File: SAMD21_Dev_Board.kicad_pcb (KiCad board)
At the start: 2 copper layers, 55.4 x 87.4 mm, 88 parts, among them J1 SWD, J10 JST_SH_SM06B-SRSS-TB_1x06-1MP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, J11 JST_SH_SM06B-SRSS-TB_1x06-1MP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, J12 JST_SH_SM06B-SRSS-TB_1x06-1MP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, J13 JST_SH_SM06B-SRSS-TB_1x06-1MP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, J14 JST_SH_SM06B-SRSS-TB_1x06-1MP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, J15 JST_SH_SM06B-SRSS-TB_1x06-1MP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, J16 JST_SH_SM06B-SRSS-TB_1x06-1MP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, J17 Status LED, J2 USB_C_Receptacle_USB2.0_16P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

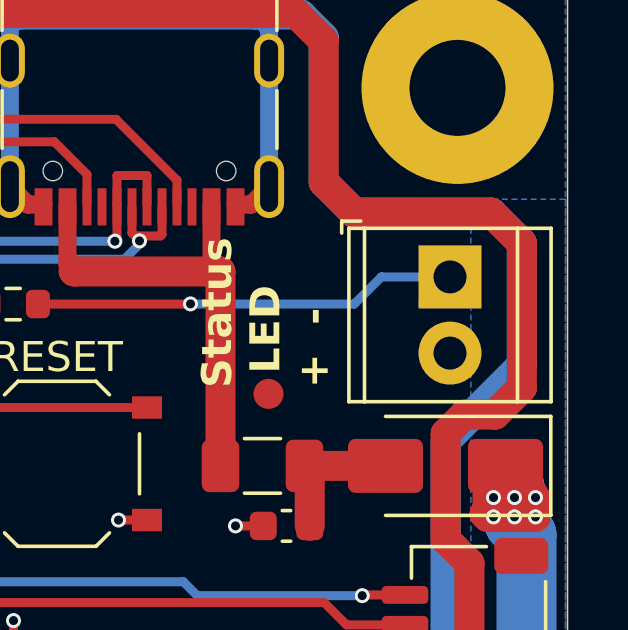
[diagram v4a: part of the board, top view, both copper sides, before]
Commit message: Increase solder paste opennings by 5% for elect.capacitor and headers. Decrease screw terminal holes from 1.1mm to 1.0mm.
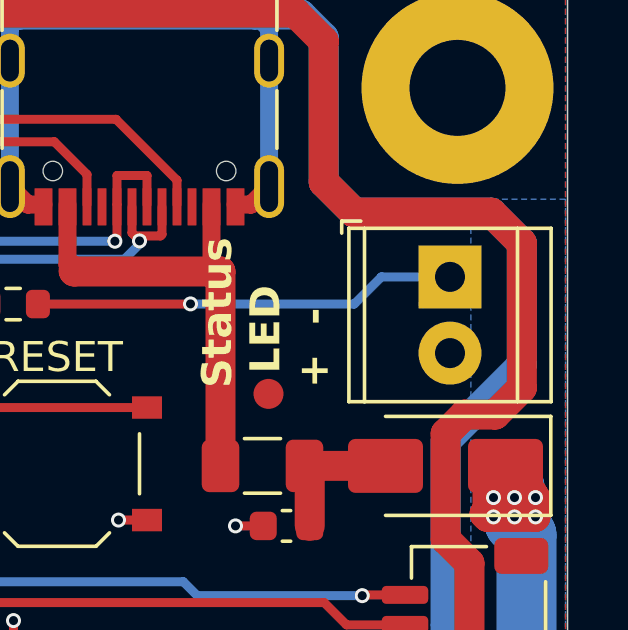
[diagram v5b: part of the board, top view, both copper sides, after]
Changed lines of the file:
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@@
 	(net 72 "D23")
 	(net 73 "D38")
-	(net 74 "unconnected-(J3-Pin_1-Pad1)_1")
-	(net 75 "unconnected-(J4-Pin_3-Pad3)")
-	(net 76 "unconnected-(J5-Pin_3-Pad3)")
-	(net 77 "unconnected-(J6-Pin_3-Pad3)")
-	(net 78 "unconnected-(J20-Pin_3-Pad3)")
-	(net 79 "unconnected-(J4-Pin_3-Pad3)_1")
-	(net 80 "unconnected-(J5-Pin_3-Pad3)_1")
-	(net 81 "unconnected-(J6-Pin_3-Pad3)_1")
-	(net 82 "unconnected-(J20-Pin_3-Pad3)_1")
-	(net 83 "unconnected-(J3-Pin_1-Pad1)")
-	(net 84 "unconnected-(J3-Pin_1-Pad1)_2")
-	(net 85 "D22")
-	(net 86 "D31")
+	(net 74 "unconnected-(J5-Pin_3-Pad3)")
+	(net 75 "unconnected-(J6-Pin_3-Pad3)")
+	(net 76 "unconnected-(J4-Pin_3-Pad3)_1")
+	(net 77 "unconnected-(J20-Pin_3-Pad3)_1")
+	(net 78 "unconnected-(J3-Pin_1-Pad1)")
+	(net 79 "D22")
+	(net 80 "D31")
 	(footprint "Capacitor_SMD:C_0603_1608Metric"
 		(layer "F.Cu")
@@
 			(layers "F.Cu" "F.Paste" "F.Mask")
 			(roundrect_rratio 0.25)
-			(net 85 "D22")
+			(net 79 "D22")
 			(pinfunction "Pin_6")
 			(pintype "passive")
@@
 			(at 0 0 270)
 			(size 2.1 2.1)
-			(drill 1.1)
+			(drill 1)
 			(layers "*.Cu" "*.Mask" "In1.Cu" "In2.Cu" "In3.Cu" "In4.Cu" "In5.Cu" "In6.Cu"
 				"In7.Cu" "In8.Cu" "In9.Cu" "In10.Cu" "In11.Cu" "In12.Cu" "In13.Cu" "In14.Cu"
@@
 			(at 2.54 0 270)
 			(size 2.1 2.1)
-			(drill 1.1)
+			(drill 1)
 			(layers "*.Cu" "*.Mask" "In1.Cu" "In2.Cu" "In3.Cu" "In4.Cu" "In5.Cu" "In6.Cu"
 				"In7.Cu" "In8.Cu" "In9.Cu" "In10.Cu" "In11.Cu" "In12.Cu" "In13.Cu" "In14.Cu"
@@
 			(layers "F.Cu" "F.Paste" "F.Mask")
 			(roundrect_rratio 0.25)
-			(net 85 "D22")
+			(net 79 "D22")
 			(pinfunction "PA12")
 			(pintype "bidirectional")
@@
 			(layers "F.Cu" "F.Paste" "F.Mask")
 			(roundrect_rratio 0.25)
-			(net 86 "D31")
+			(net 80 "D31")
 			(pinfunction "PB23")
 			(pintype "bidirectional+no_connect")
@@
 		(sheetname "Root")
 		(sheetfile "SAMD21_Dev_Board.kicad_sch")
+		(solder_paste_ratio 0.05)
 		(attr smd)
 		(fp_line
@@
 			(size 1.9 1)
 			(layers "F.Cu" "F.Paste" "F.Mask")
-			(net 83 "unconnected-(J3-Pin_1-Pad1)")
+			(net 78 "unconnected-(J3-Pin_1-Pad1)")
 			(pinfunction "Pin_1")
 			(pintype "passive+no_connect")
@@
 			(remove_unused_layers no)
 			(roundrect_rratio 0.2083333333)
-			(net 84 "unconnected-(J3-Pin_1-Pad1)_2")
+			(net 78 "unconnected-(J3-Pin_1-Pad1)")
 			(pinfunction "Pin_1")
 			(pintype "passive+no_connect")
@@
 			(size 1.9 1)
 			(layers "F.Cu" "F.Paste" "F.Mask")
-			(net 74 "unconnected-(J3-Pin_1-Pad1)_1")
+			(net 78 "unconnected-(J3-Pin_1-Pad1)")
 			(pinfunction "Pin_1")
 			(pintype "passive+no_connect")
@@
 		(sheetname "Root")
 		(sheetfile "SAMD21_Dev_Board.kicad_sch")
+		(solder_paste_ratio 0.05)
 		(attr smd)
 		(fp_line
@@
 			(remove_unused_layers no)
 			(roundrect_rratio 0.2083333333)
-			(net 76 "unconnected-(J5-Pin_3-Pad3)")
+			(net 74 "unconnected-(J5-Pin_3-Pad3)")
 			(pinfunction "Pin_3")
 			(pintype "passive+no_connect")
@@
 			(size 1.9 1)
 			(layers "F.Cu" "F.Paste" "F.Mask")
-			(net 80 "unconnected-(J5-Pin_3-Pad3)_1")
+			(net 74 "unconnected-(J5-Pin_3-Pad3)")
 			(pinfunction "Pin_3")
 			(pintype "passive+no_connect")
@@
 		(sheetname "Root")
 		(sheetfile "SAMD21_Dev_Board.kicad_sch")
+		(solder_paste_ratio 0.05)
 		(attr smd)
 		(fp_line
@@
 		(sheetname "Root")
 		(sheetfile "SAMD21_Dev_Board.kicad_sch")
+		(solder_paste_ratio 0.05)
 		(attr smd)
 		(fp_line
@@
 			(remove_unused_layers no)
 			(roundrect_rratio 0.2083333333)
-			(net 82 "unconnected-(J20-Pin_3-Pad3)_1")
+			(net 77 "unconnected-(J20-Pin_3-Pad3)_1")
 			(pinfunction "Pin_3")
 			(pintype "passive+no_connect")
@@
 			(size 1.9 1)
 			(layers "F.Cu" "F.Paste" "F.Mask")
-			(net 78 "unconnected-(J20-Pin_3-Pad3)")
+			(net 77 "unconnected-(J20-Pin_3-Pad3)_1")
 			(pinfunction "Pin_3")
 			(pintype "passive+no_connect")
@@
 		(sheetname "Root")
 		(sheetfile "SAMD21_Dev_Board.kicad_sch")
+		(solder_paste_ratio 0.05)
 		(attr smd)
 		(fp_line
@@
 			(size 1.9 1)
 			(layers "F.Cu" "F.Paste" "F.Mask")
-			(net 77 "unconnected-(J6-Pin_3-Pad3)")
+			(net 75 "unconnected-(J6-Pin_3-Pad3)")
 			(pinfunction "Pin_3")
 			(pintype "passive+no_connect")
@@
 			(remove_unused_layers no)
 			(roundrect_rratio 0.2083333333)
-			(net 81 "unconnected-(J6-Pin_3-Pad3)_1")
+			(net 75 "unconnected-(J6-Pin_3-Pad3)")
 			(pinfunction "Pin_3")
 			(pintype "passive+no_connect")
@@
 		(sheetname "Root")
 		(sheetfile "SAMD21_Dev_Board.kicad_sch")
+		(solder_paste_ratio 0.05)
 		(attr smd)
 		(fp_line
@@
 			(size 1.9 1)
 			(layers "F.Cu" "F.Paste" "F.Mask")
-			(net 79 "unconnected-(J4-Pin_3-Pad3)_1")
+			(net 76 "unconnected-(J4-Pin_3-Pad3)_1")
 			(pinfunction "Pin_3")
 			(pintype "passive+no_connect")
@@
 			(remove_unused_layers no)
 			(roundrect_rratio 0.2083333333)
-			(net 75 "unconnected-(J4-Pin_3-Pad3)")
+			(net 76 "unconnected-(J4-Pin_3-Pad3)_1")
 			(pinfunction "Pin_3")
 			(pintype "passive+no_connect")
@@
 		(width 0.3)
 		(layer "F.Cu")
-		(net 85)
+		(net 79)
 	)
 	(segment
@@
 		(width 0.3)
 		(layer "F.Cu")
-		(net 85)
+		(net 79)
 	)
 	(segment
@@
 		(width 0.3)
 		(layer "F.Cu")
-		(net 85)
+		(net 79)
 	)
 	(via
@@
 		(drill 0.3)
 		(layers "F.Cu" "B.Cu")
-		(net 85)
+		(net 79)
 	)
 	(via
@@
 		(drill 0.3)
 		(layers "F.Cu" "B.Cu")
-		(net 85)
+		(net 79)
 	)
 	(segment
@@
 		(width 0.3)
 		(layer "B.Cu")
-		(net 85)
+		(net 79)
 	)
 	(segment
@@
 		(width 0.3)
 		(layer "B.Cu")
-		(net 85)
+		(net 79)
 	)
 	(segment
@@
 		(width 0.3)
 		(layer "B.Cu")
-		(net 85)
+		(net 79)
 	)
 	(segment
@@
 		(width 0.3)
 		(layer "B.Cu")
-		(net 85)
+		(net 79)
 	)
 	(segment
@@
 		(width 0.3)
 		(layer "B.Cu")
-		(net 85)
+		(net 79)
 	)
 	(segment
@@
 		(width 0.3)
 		(layer "B.Cu")
-		(net 85)
+		(net 79)
 	)
 	(zone
@@
 	)
 	(group ""
-		(members "36dbe753-2aa2-4a08-bfe0-0553d9ccbec4" "dd14f451-9a5a-4539-8c54-8018feec234c")
-	)
-	(group ""
